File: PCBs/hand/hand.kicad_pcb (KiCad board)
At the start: 4 copper layers, 108.4 x 88 mm, 81 parts, among them J5 Conn_02x04_Odd_Even, J6 Conn_01x02, U1 TJA1057GT/3J, U2 STM32F303RETx, U3 LM317_TO-220, U4 LM317_TO-220, U5 LSM6DSMTR

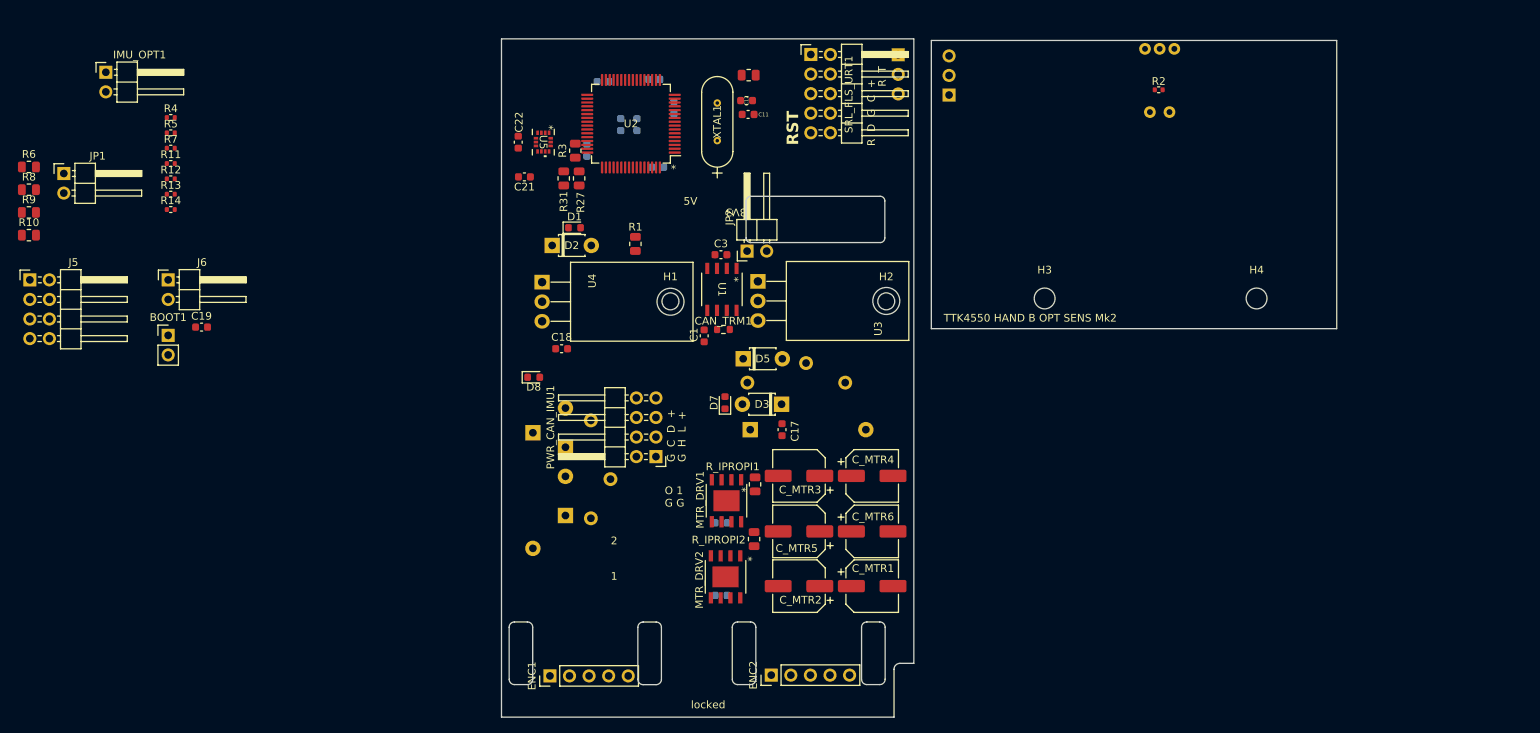
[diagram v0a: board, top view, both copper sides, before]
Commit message: Updated ign with ever more variations of autosaves. Finished tracing hand, probably need new footprint for encoders. Next up: find footprints, redo IMU board
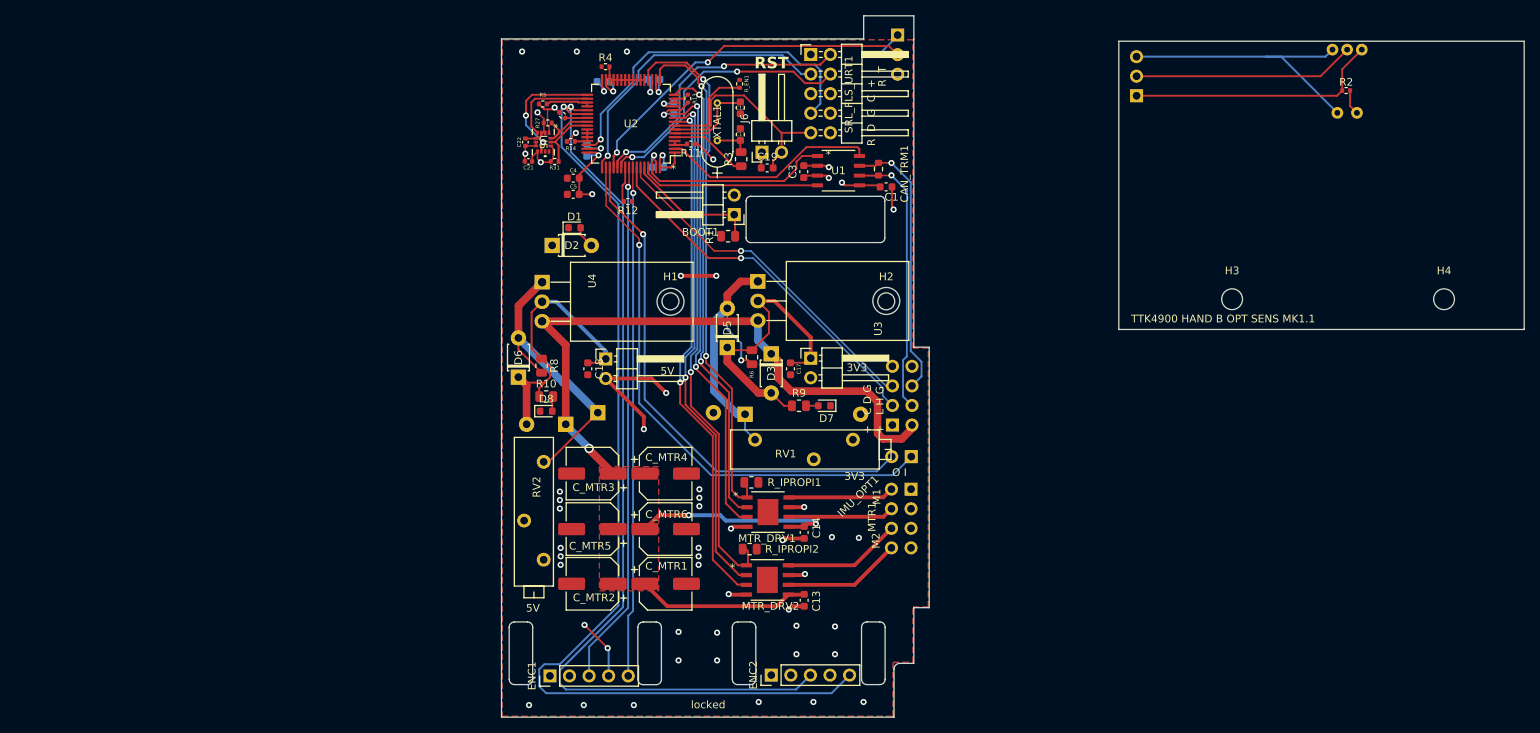
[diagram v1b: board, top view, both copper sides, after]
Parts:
- BOOT1: footprint Connector_PinHeader_2.54mm:PinHeader_1x02_P2.54mm_Vertical -> Connector_PinHeader_2.54mm:PinHeader_1x02_P2.54mm_Horizontal
- C13, C14, C4, C5, D6, RV1, RV2: moved to F.Cu
- C21, C22: footprint Capacitor_SMD:C_0603_1608Metric -> Capacitor_SMD:C_0402_1005Metric
- IMU_OPT1: footprint Connector_PinHeader_2.54mm:PinHeader_1x02_P2.54mm_Horizontal -> Connector_PinHeader_2.54mm:PinHeader_1x02_P2.54mm_Vertical; moved to B.Cu
- MTR1: renamed from J5; footprint Connector_PinHeader_2.54mm:PinHeader_2x04_P2.54mm_Horizontal -> Connector_PinHeader_2.54mm:PinHeader_2x04_P2.54mm_Vertical; moved to B.Cu
- PWR_CAN_IMU1: footprint Connector_PinHeader_2.54mm:PinHeader_2x04_P2.54mm_Horizontal -> Connector_PinHeader_2.54mm:PinHeader_2x04_P2.54mm_Vertical; moved to B.Cu
- R27, R31, R_EN1: footprint Resistor_SMD:R_0805_2012Metric -> Resistor_SMD:R_0402_1005Metric
- moved MTR1 117.5 mm to (78.7, 79.7), turned to 180 degrees
- moved IMU_OPT1 115.8 mm to (78.7, 75.5), turned to 90 degrees
- moved R9 103.0 mm to (64.1, 68.9)
- moved JP1 99.8 mm to (65.7, 62.7)
- moved R6 97.0 mm to (58.0, 62.6), turned to -90 degrees
- moved J6 78.8 mm to (59.3, 36.0), turned to 90 degrees
- moved C19 76.2 mm to (60.0, 38.0)
- moved BOOT1 75.1 mm to (55.7, 44.1), turned to 180 degrees
- moved R8 70.3 mm to (30.7, 63.7), turned to -90 degrees
- moved R10 70.3 mm to (31.3, 67.7)
- moved R13 68.2 mm to (49.7, 29.0), turned to 90 degrees
- moved R11 67.5 mm to (50.1, 34.9), turned to 180 degrees
- moved R12 59.4 mm to (41.9, 42.4), turned to 180 degrees
- moved R4 56.8 mm to (39.0, 24.9)
- moved R14 52.7 mm to (34.5, 34.6)
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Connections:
- C4 pad 1: Net-(D1-A) -> +3V3
- C5 pad 1: Net-(D1-A) -> +3V3
- IMU_OPT1 pad 1: /OPT_SW2 -> /IMU_INT3
- IMU_OPT1 pad 2: /IMU_INT3 -> /OPT_SW2
- MTR1 pad 2: Net-(J5-Pin_2) -> Net-(MTR1-Pin_2)
- MTR1 pad 4: Net-(J5-Pin_4) -> Net-(MTR1-Pin_4)
- MTR1 pad 6: Net-(J5-Pin_6) -> Net-(MTR1-Pin_6)
- MTR1 pad 8: Net-(J5-Pin_8) -> Net-(MTR1-Pin_8)
- MTR_DRV1 pad 6: Net-(J5-Pin_2) -> Net-(MTR1-Pin_4)
- MTR_DRV1 pad 8: Net-(J5-Pin_4) -> Net-(MTR1-Pin_2)
- MTR_DRV2 pad 6: Net-(J5-Pin_6) -> Net-(MTR1-Pin_8)
- MTR_DRV2 pad 8: Net-(J5-Pin_8) -> Net-(MTR1-Pin_6)
- PWR_CAN_IMU1 pad 1: GND -> +5V
- PWR_CAN_IMU1 pad 2: GND -> +48V
- PWR_CAN_IMU1 pad 3: /I2C3_SCL -> /I2C1_SCL
- PWR_CAN_IMU1 pad 4: /CANH -> /CANL
- PWR_CAN_IMU1 pad 5: /I2C3_SDA -> /I2C1_SDA
- PWR_CAN_IMU1 pad 6: /CANL -> /CANH
- PWR_CAN_IMU1 pad 7: +5V -> GND
- PWR_CAN_IMU1 pad 8: +48V -> GND
- R27 pad 2: /I2C1_SDA -> /I2C3_SDA
- R31 pad 2: /I2C1_SCL -> /I2C3_SCL
- U5 pad 13: /I2C1_SCL -> /I2C3_SCL
- U5 pad 14: /I2C1_SDA -> /I2C3_SDA
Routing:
- net +48V: track 0.00 -> 133.8 mm, vias 0 -> 3
- net /ENC2A: track 0.00 -> 128.9 mm, vias 0 -> 1
- net /ENC2B: track 0.00 -> 117.0 mm, vias 0 -> 1
- net GND: track 0.00 -> 85.5 mm, vias 0 -> 46
- net +5V: track 0.00 -> 74.2 mm, vias 0 -> 7
- net /IMU_INT3: track 0.00 -> 72.5 mm, vias 0 -> 1
- net /DRV2_IPROPI: track 0.00 -> 69.6 mm, vias 0 -> 2
- net /DRV1_IPROPI: track 0.00 -> 69.4 mm, vias 0 -> 2
- net /OPT_SW2: track 0.00 -> 68.7 mm, vias 0 -> 1
- net /ENC1B: track 0.00 -> 68.1 mm, vias 0 -> 1
- net /DRV2_IN1: track 0.00 -> 67.0 mm, vias 0 -> 2
- net /DRV2_IN2: track 0.00 -> 66.8 mm, vias 0 -> 2
- net /DRV1_IN2: track 0.00 -> 66.7 mm, vias 0 -> 2
- net /ENC1A: track 0.00 -> 66.3 mm, vias 0 -> 1
- net /DRV1_IN1: track 0.00 -> 62.6 mm, vias 0 -> 2
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- added copper zone on In2.Cu, net +3V3
- added copper zone on F.Cu, net +48V
- added copper zone on B.Cu, net +5V
- added copper zone on F.Cu, net GND
- added copper zone on In1.Cu, net GND
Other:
- board size 108.4 x 88 mm -> 132.7 x 91 mm
- board text added: "+ C D G + L H G"
- board text added: "M1"
- board text added: "M2"
- board text added: "O I"
- board text added: "TTK4900 HAND B OPT SENS MK1.1"
- board text removed: "1"
- board text removed: "2"
- board text removed: "G C D +"
- board text removed: "G H L +"
- board text removed: "O 1 G G"
- board text removed: "TTK4550 HAND B OPT SENS Mk2"

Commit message: All revisions finished, MK1.1 ready for gerber generation
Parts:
- ENC1, ENC2: footprint Connector_PinHeader_2.54mm:PinHeader_1x05_P2.54mm_Vertical -> PINSOCKET:PinSocket_1x05_P2.54mm_Vertical
- moved ENC1 0.40 mm to (31.4, 103.9)
- moved ENC2 0.20 mm to (60.3, 103.8)
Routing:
- net /ENC2A: track 128.9 -> 109.3 mm, vias 1 -> 3
- net /ENC2B: track 117.0 -> 100.8 mm, vias 1 -> 3

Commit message: Separated Hand B as separate Kicad project. Next up: gerber generation
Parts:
- removed CON_B1: Conn_01x03, Connector_PinHeader_2.54mm:PinHeader_1x03_P2.54mm_Vertical
- removed H3, H4: MountingHole, MountingHole:MountingHole_2.7mm_M2.5
- removed OPT1: ~, OPB971N51:OPB971N51
- removed R2: 220, Resistor_SMD:R_0402_1005Metric
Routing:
- net +5V: track 74.2 -> 36.1 mm
- net GND: track 85.5 -> 52.2 mm
- net /OPT_assy/OPT_B: track 28.8 -> 0.00 mm
- net Net-(OPT1-Cathode): track 3.26 -> 0.00 mm
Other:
- board size 132.7 x 91 mm -> 55.5 x 91 mm
- board text removed: "TTK4900 HAND B OPT SENS MK1.1"
